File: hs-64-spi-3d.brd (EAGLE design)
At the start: 19.3 x 18.8 mm, 30 parts, among them J1 DF40C-70DP-0.4V(51), J2 A79622-001, U1 RHD2064_BGA, U2 BNO055, U3 TLV70725

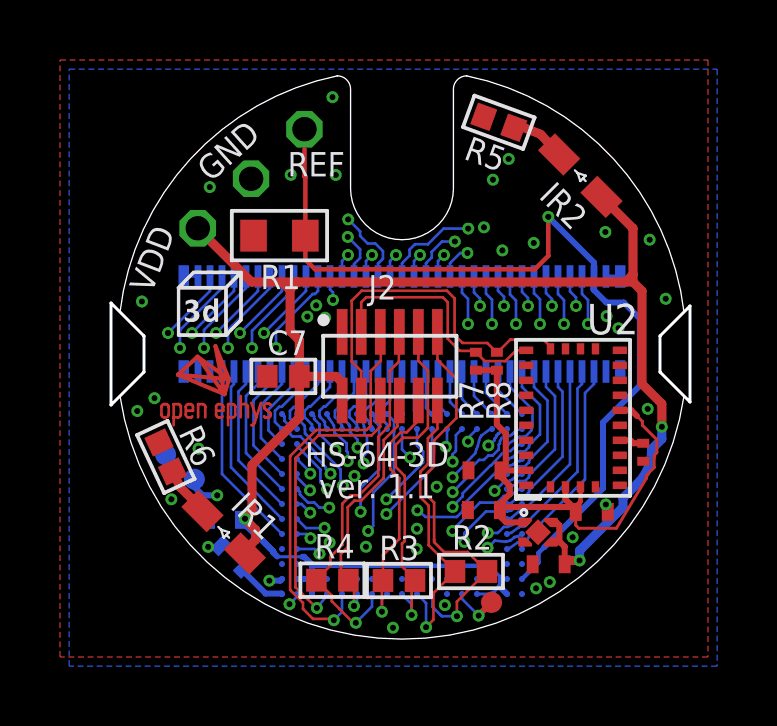
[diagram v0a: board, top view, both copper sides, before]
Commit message: Added EEPROM.
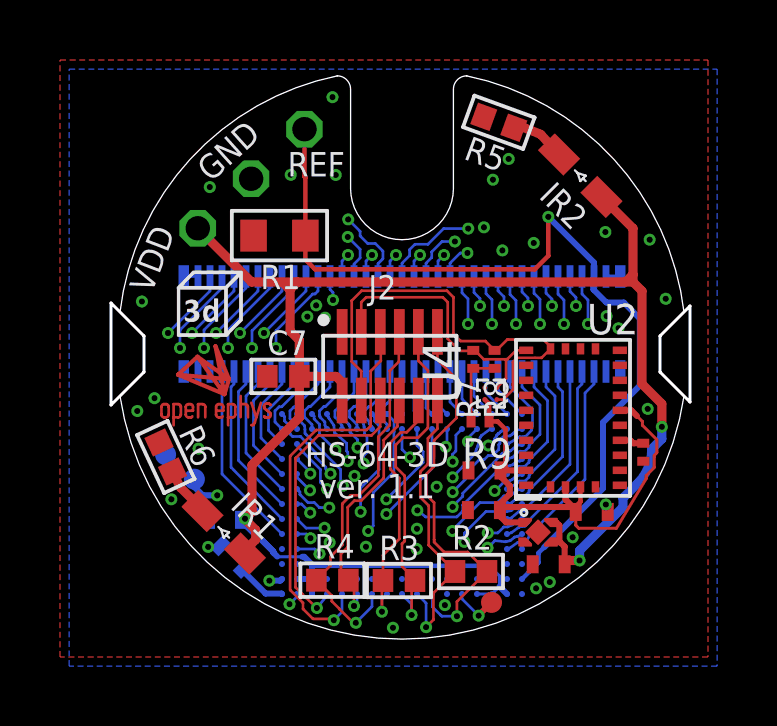
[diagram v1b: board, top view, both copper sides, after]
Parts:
- added R9: 0, jonnew:0201T
- added U4: 24CW640T-I/CS0668, 24CW640T-I_CS0668:4-BALL_WAFFER_0.4MMX0.4MM
- moved R7 0.11 mm to (2.37, -0.18)
- moved R8 0.10 mm to (3.09, -0.18)
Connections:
- new net N$1: R7.1, R8.1, R9.2
- net +2V5: now also R9.1, U4.A1; no longer R7.1, R8.1
- net AGND: now also U4.A2
- net BNO_SCL: now also U4.B1
- net BNO_SDA: now also U4.B2
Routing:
- net BNO_SCL: track 12.1 -> 15.1 mm
- net N$1: track 0.00 -> 2.51 mm
- net +2V5: track 19.2 -> 17.9 mm
- net BNO_SDA: track 8.31 -> 9.35 mm
